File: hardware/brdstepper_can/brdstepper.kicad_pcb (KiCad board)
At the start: 4 copper layers, 28 x 28 mm, 94 parts, among them J1 USB-C, J2 VM / GND / EN, J3 MOTOR, J4 SMART-SERIAL, J5 CAN, J6 CAN, J7 SWD, U1 STM32G473CEU6, U2 DRV8876RGTR, U3 DRV8876RGTR, U4 AS5047P-ATSM, U5 TLV75533PDBVR, U6 TPS560430XDBVR, U7 USBLC6-2SC6, U8 SN65HVD30DR, U9 TCAN1044VDR, Y1 8MHz

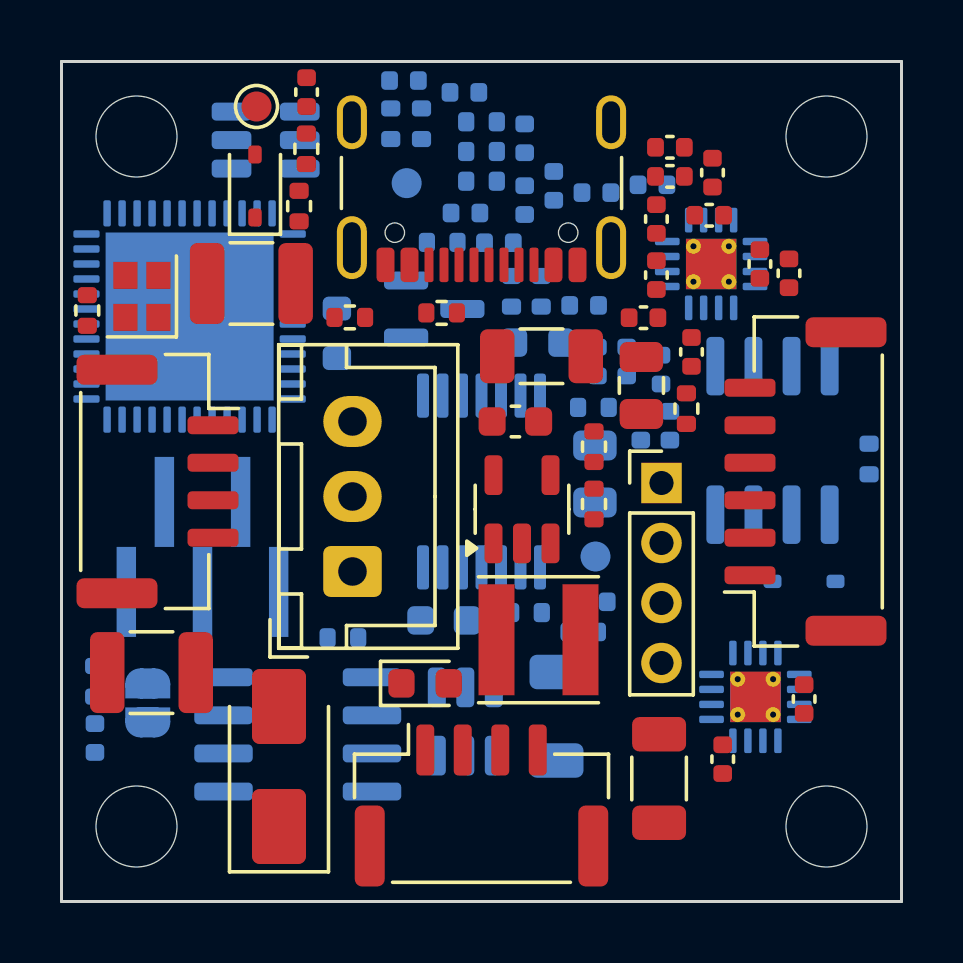
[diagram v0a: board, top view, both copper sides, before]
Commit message: brdstepper: split into serial and CAN boards, 0603 passives (WIP, not routed)
- hardware/brdstepper_common: shared parts/board definitions built per
  variant; brdstepper_mesa (A, smart-serial) and brdstepper_can (B, CAN)
  each fit only their own interface parts, MCU pins of the other
  interface left open, HWID divider per variant.
- 0402 resistors and capacitors become 0603; power capacitors stay larger.
- kigen place: GAP_MAX bisects the largest courtyard gap that still
  places every part (0603 on 28 x 28 mm only just fits: gap ~0).
- kigen route: DSN export, BrdRoute, SES import, zone fill (untested end
  to end: first router run still going).

Not done yet: routing on 4 layers, READMEs/BOMs/renders refresh, DEBUGNOTES.

Co-Authored-By: Claude Sonnet 5.5 <noreply@anthropic.com>
Claude-Session: https://claude.ai/code/session_017CSpK2B8oMBAmr39Kq1RSC
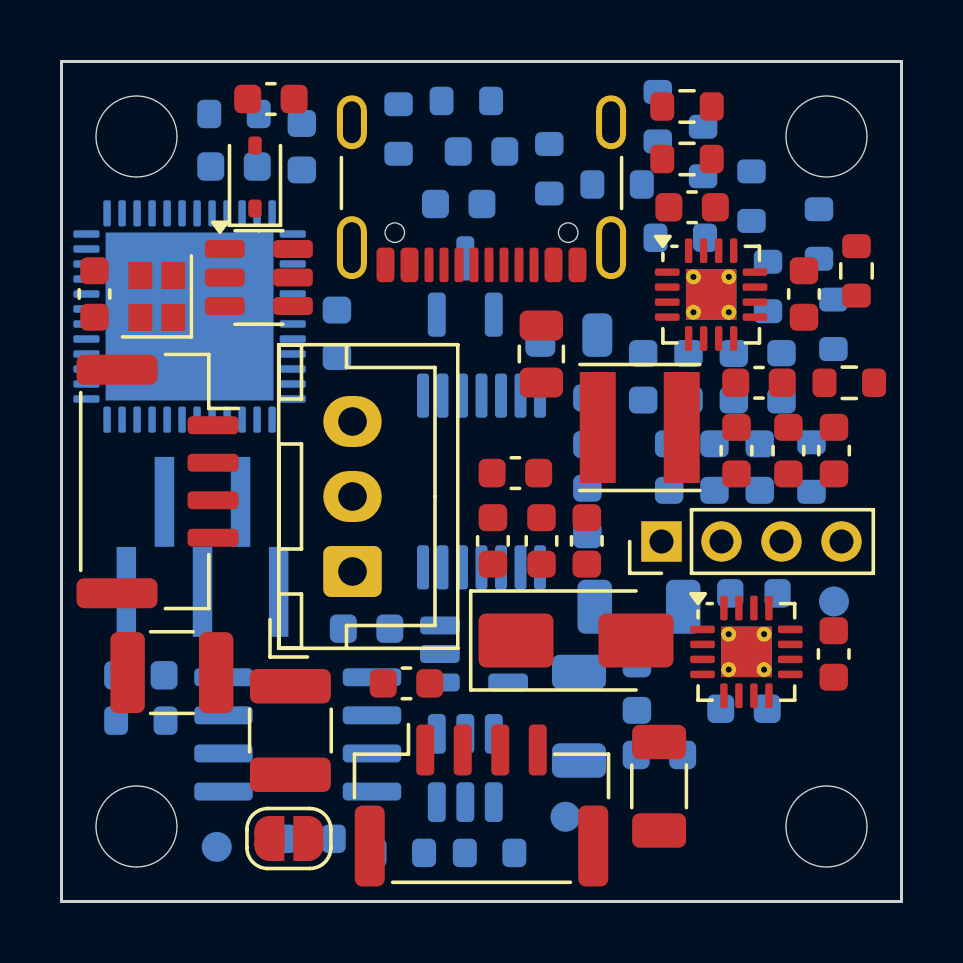
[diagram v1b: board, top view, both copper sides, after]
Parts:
- removed C38: 100n, Capacitor_SMD:C_0402_1005Metric
- removed D3: BAT54WS, Diode_SMD:D_SOD-323
- removed J4: SMART-SERIAL, Connector_JST:JST_GH_SM06B-GHS-TB_1x06-1MP_P1.25mm_Horizontal
- removed R20: 120, Resistor_SMD:R_0402_1005Metric
- removed U8: SN65HVD30DR, Package_SO:SOIC-8_3.9x4.9mm_P1.27mm
- C10, C12, C13, C18, C22, C27, C39, C9: footprint Capacitor_SMD:C_0402_1005Metric -> Capacitor_SMD:C_0603_1608Metric; moved to F.Cu
- C11, C14, C15, C16, C17, C19, C25, C26, C29, C31, C32, C33, C34, C36, C37, C5: footprint Capacitor_SMD:C_0402_1005Metric -> Capacitor_SMD:C_0603_1608Metric
- C20, C23, C30, C4, C40, C8: footprint Capacitor_SMD:C_0402_1005Metric -> Capacitor_SMD:C_0603_1608Metric; moved to B.Cu
- C21, C3, C7, D4, TP2, U5: moved to B.Cu
- C6, JP1, U2, U3, U7: moved to F.Cu
- R1, R10, R11, R14, R15, R16, R3: footprint Resistor_SMD:R_0402_1005Metric -> Resistor_SMD:R_0603_1608Metric; moved to B.Cu
- R12, R18, R19, R2, R21, R4, R5, R6, R7, R9: footprint Resistor_SMD:R_0402_1005Metric -> Resistor_SMD:R_0603_1608Metric
- R13, R17, R8: footprint Resistor_SMD:R_0402_1005Metric -> Resistor_SMD:R_0603_1608Metric; moved to F.Cu
- moved TP2 24.7 mm to (91.2, 112.2)
- moved TP3 21.8 mm to (102.8, 111.2)
- moved R4 20.4 mm to (97.3, 112.4)
- moved C4 18.0 mm to (105.2, 106.9), turned to 90 degrees
- moved TH1 16.6 mm to (111.7, 94.8)
- moved R8 15.3 mm to (112.5, 93.0)
- moved C18 15.0 mm to (97.5, 106.7)
- moved C1 15.0 mm to (93.6, 108.3), turned to 90 degrees
- moved R5 14.4 mm to (100.3, 112.4), turned to 0 degrees
- moved R3 13.8 mm to (88.6, 108.0), turned to 0 degrees
- moved C19 12.4 mm to (96.2, 104.9), turned to 0 degrees
- moved R7 12.3 mm to (109.0, 90.5)
- moved D4 11.4 mm to (109.1, 103.7)
- moved D2 10.8 mm to (103.2, 105.3), turned to 0 degrees
- moved C9 10.7 mm to (111.8, 99.0), turned to 90 degrees
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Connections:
- U1 pad 44: SS_TX -> (no net)
- U1 pad 45: SS_RX -> (no net)

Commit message: brdstepper: re-placed boards without J2 (routing run in progress)
Both boards re-placed with J2 gone, courtyard gap 0.40 mm. Snapshot taken
while the first plane-aware routing run is still going: copper may be
missing or partial.

Co-Authored-By: Claude Sonnet 5.5 <noreply@anthropic.com>
Claude-Session: https://claude.ai/code/session_017CSpK2B8oMBAmr39Kq1RSC
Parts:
- removed C37: 4.7n, Capacitor_SMD:C_0603_1608Metric
- removed J1: USB-C, Connector_USB:USB_C_Receptacle_GCT_USB4105-xx-A_16P_TopMnt_Horizontal
- removed J2: VM / GND / EN, Connector_JST:JST_XH_B3B-XH-A_1x03_P2.50mm_Vertical
- removed J7: SWD, Connector_PinHeader_1.27mm:PinHeader_1x05_P1.27mm_Vertical_SMD_Pin1Left
- removed R17, R18: 5.1k, Resistor_SMD:R_0603_1608Metric
- removed R19: 1M, Resistor_SMD:R_0603_1608Metric
- removed U7: USBLC6-2SC6, Package_TO_SOT_SMD:SOT-23-6
- added TP10: USB D+, TestPoint:TestPoint_Pad_D1.0mm, F.Cu at (87.6, 107.0)
- added TP11: USB D-, TestPoint:TestPoint_Pad_D1.0mm, F.Cu at (93.0, 112.6)
- added TP12: USB GND, TestPoint:TestPoint_Pad_D1.0mm, B.Cu at (112.5, 102.3)
- added TP4: SWD 3V3, TestPoint:TestPoint_Pad_D1.0mm, B.Cu at (112.5, 99.5)
- added TP5: SWDIO, TestPoint:TestPoint_Pad_D1.0mm, F.Cu at (112.2, 106.9)
- added TP6: NRST, TestPoint:TestPoint_Pad_D1.0mm, B.Cu at (108.2, 112.3)
- added TP7: SWCLK, TestPoint:TestPoint_Pad_D1.0mm, B.Cu at (112.3, 105.2)
- added TP8: SWD GND, TestPoint:TestPoint_Pad_D1.0mm, B.Cu at (112.2, 108.0)
- added TP9: USB 5V, TestPoint:TestPoint_Pad_D1.0mm, B.Cu at (105.5, 112.7)
- C11, C13, C18, C22, C27, C28, C39, C6, JP1, R12, R13, R8: moved to B.Cu
- C19, C21, C3, C30, C5, C7, C8, D1, R1, R14, R3, R7, TP2, U5: moved to F.Cu
- J5, J6: footprint Connector_JST:JST_GH_SM04B-GHS-TB_1x04-1MP_P1.25mm_Horizontal -> Connector_JST:JST_GH_SM05B-GHS-TB_1x05-1MP_P1.25mm_Horizontal
- moved R3 27.1 mm to (113.0, 96.0), turned to 90 degrees
- moved R4 25.6 mm to (112.9, 92.2), turned to 90 degrees
- moved R9 24.2 mm to (99.5, 113.0), turned to 0 degrees
- moved R16 24.1 mm to (92.3, 110.3)
- moved R2 22.9 mm to (92.2, 112.7), turned to 0 degrees
- moved R1 22.2 mm to (93.1, 109.5), turned to 90 degrees
- moved R15 22.1 mm to (87.9, 108.3), turned to 0 degrees
- moved R7 18.6 mm to (107.0, 109.0)
- moved R10 18.1 mm to (87.1, 105.2), turned to 90 degrees
- moved J3 17.2 mm to (97.0, 87.4)
- moved R8 17.0 mm to (106.8, 109.0)
- moved TH1 16.6 mm to (104.3, 109.5)
- moved TP2 15.7 mm to (106.9, 112.3)
- moved C5 15.2 mm to (90.9, 106.7)
- moved C19 15.1 mm to (101.3, 90.7)
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
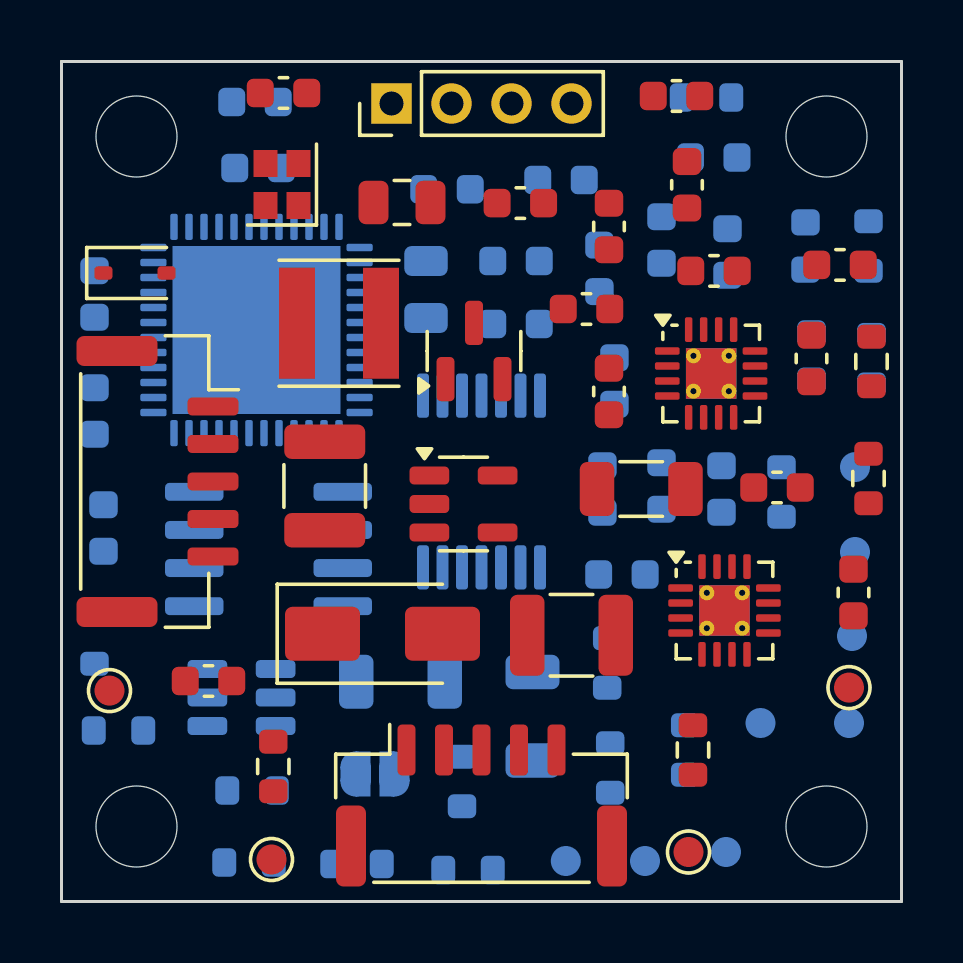
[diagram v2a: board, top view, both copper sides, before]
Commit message: brdstepper: routed snapshot with GND plane fanout, partial (WIP)
First plane-aware BrdRoute runs (150 s cap): serial 70/129 connections,
CAN 69/135, not complete, DRC not clean. Longer runs are in progress.

Co-Authored-By: Claude Sonnet 5.5 <noreply@anthropic.com>
Claude-Session: https://claude.ai/code/session_017CSpK2B8oMBAmr39Kq1RSC
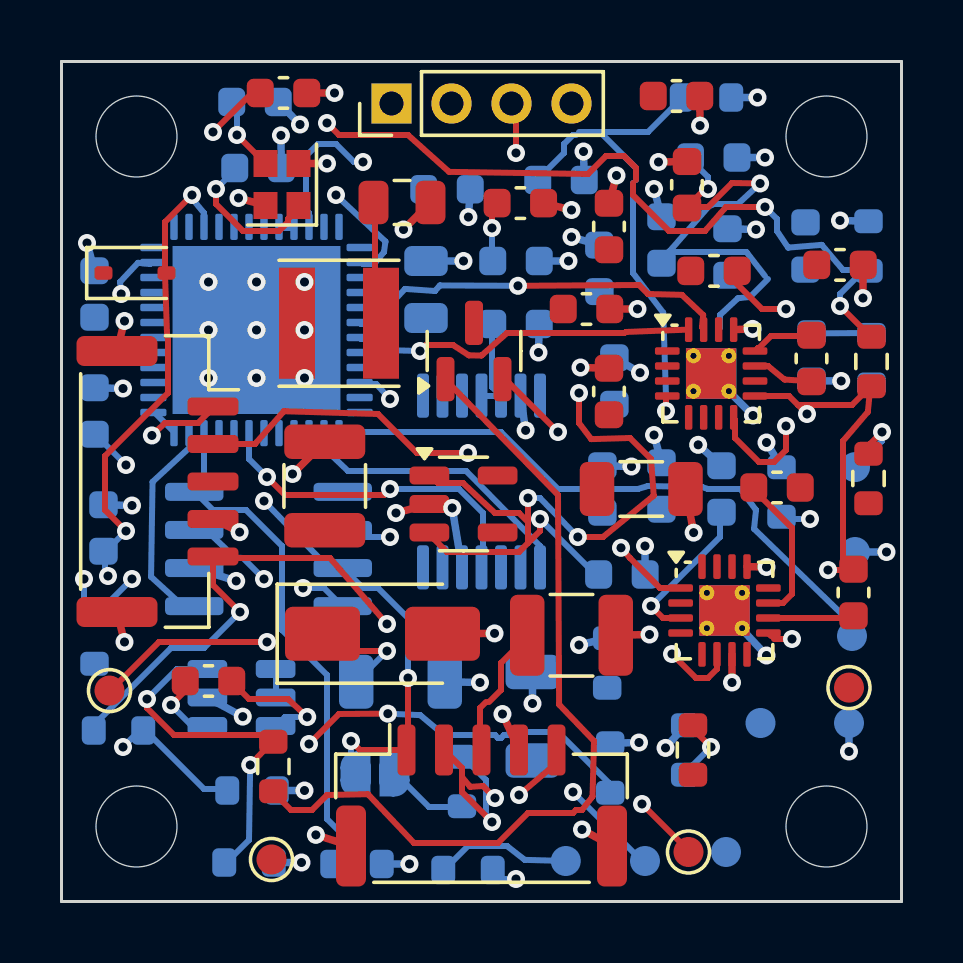
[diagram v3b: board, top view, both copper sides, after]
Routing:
- net GND: track 0.00 -> 69.4 mm, vias 0 -> 73
- net 5V: track 0.00 -> 54.8 mm, vias 0 -> 5
- net NTC: track 0.00 -> 34.9 mm, vias 0 -> 5
- net CANL: track 0.00 -> 33.2 mm, vias 0 -> 4
- net 5V_BUCK: track 0.00 -> 32.5 mm
- net TP_PB10: track 0.00 -> 32.2 mm, vias 0 -> 2
- net VM_SENSE: track 0.00 -> 31.5 mm, vias 0 -> 4
- net VM: track 0.00 -> 30.4 mm, vias 0 -> 5
- net EN_IN: track 0.00 -> 26.5 mm, vias 0 -> 4
- net EN_RAW: track 0.00 -> 25.3 mm, vias 0 -> 3
- net COIL_B+: track 0.00 -> 23.0 mm, vias 0 -> 2
- net 3V3: track 0.00 -> 23.0 mm, vias 0 -> 4
- net AIN: track 0.00 -> 22.3 mm, vias 0 -> 2
- net COIL_A-: track 0.00 -> 21.1 mm, vias 0 -> 1
- net CANH: track 0.00 -> 21.1 mm, vias 0 -> 4
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
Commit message: brdstepper: routed with 0.127 mm rules, plane fanout; ~75% complete (WIP)
Both boards routed with BrdRoute (900 s cap): serial 100/129 connections
(77.5%), CAN 100/135 (74.1%). Not complete, DRC not clean (KiCad: serial
11 clearance, 2 edge, 29 unconnected; CAN 14, 2, 35).

kigen route fixes found on the way:
- load_bare did not strip old copper (indentation): routes piled up
- the temp-dir board lost the project's design rules and net classes
  (router saw 0.2 mm clearance): project copied in, rules written back
- default board via (0.6 mm) offered next to the net class via: first only
- net classes 0.127 mm clearance, 0.15 / 0.3 mm tracks, 0.5 / 0.25 mm vias

BOM and renders regenerated.

Co-Authored-By: Claude Sonnet 5.5 <noreply@anthropic.com>
Claude-Session: https://claude.ai/code/session_017CSpK2B8oMBAmr39Kq1RSC
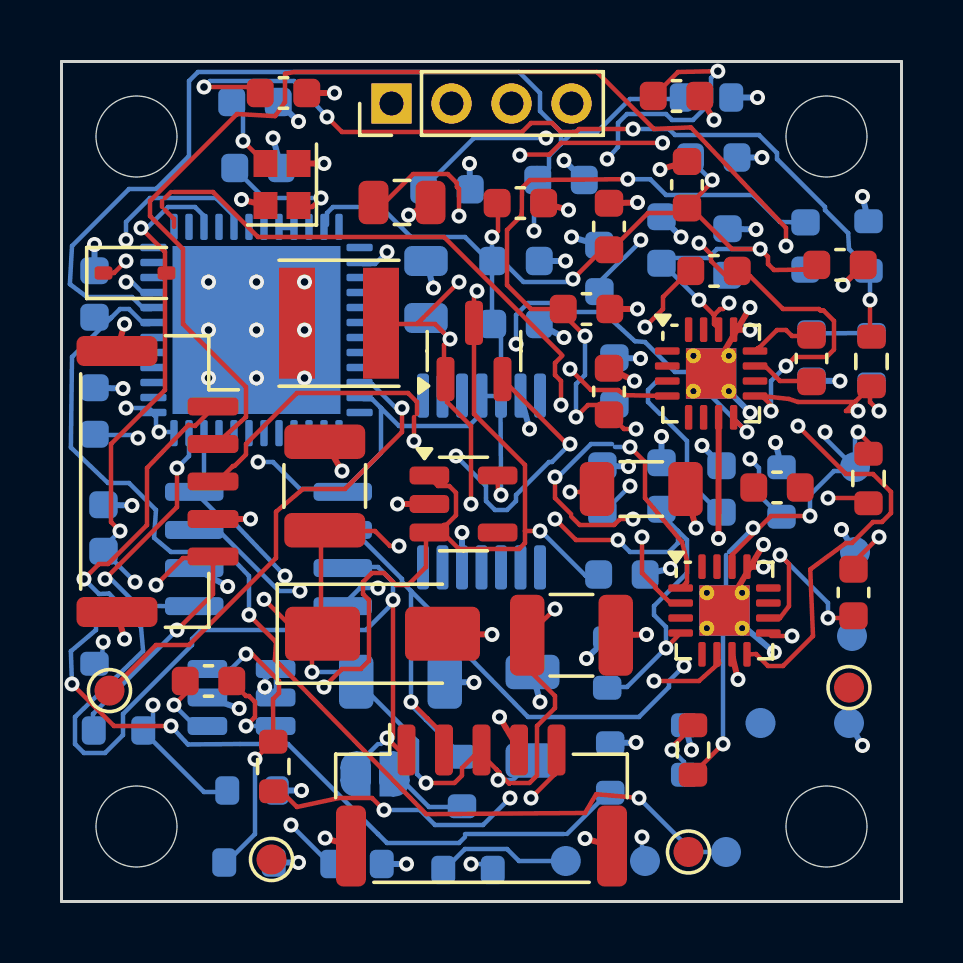
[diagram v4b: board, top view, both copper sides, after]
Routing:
- net VM: track 30.4 -> 112.8 mm, vias 5 -> 18
- net 3V3: track 23.0 -> 95.1 mm, vias 4 -> 17
- net CANL: track 33.2 -> 76.9 mm, vias 4 -> 3
- net IPROPI_B: track 0.00 -> 40.1 mm, vias 0 -> 4
- net NRST: track 0.00 -> 36.7 mm, vias 0 -> 2
- net TP_PB10: track 32.2 -> 0.00 mm, vias 2 -> 0
- net COIL_B-: track 0.00 -> 27.7 mm, vias 0 -> 1
- net IPROPI_A: track 16.6 -> 42.8 mm, vias 1 -> 2
- net VDDA: track 0.97 -> 26.9 mm, vias 0 -> 5
- net nSLEEP: track 17.0 -> 39.5 mm, vias 2 -> 5
- net SWCLK: track 20.7 -> 0.00 mm
- net CANH: track 21.1 -> 37.7 mm, vias 4 -> 3
- net U2_VCP: track 0.00 -> 15.8 mm, vias 0 -> 3
- net A_IN1: track 13.0 -> 0.00 mm, vias 1 -> 0
- net AIN: track 22.3 -> 35.1 mm, vias 2 -> 3
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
